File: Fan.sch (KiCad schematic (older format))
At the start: 11 parts, among them Q2 DMN65D8L-7, Q3 AOD476, Q4 AOD476, U4 OPA4170, U5 MCP4801

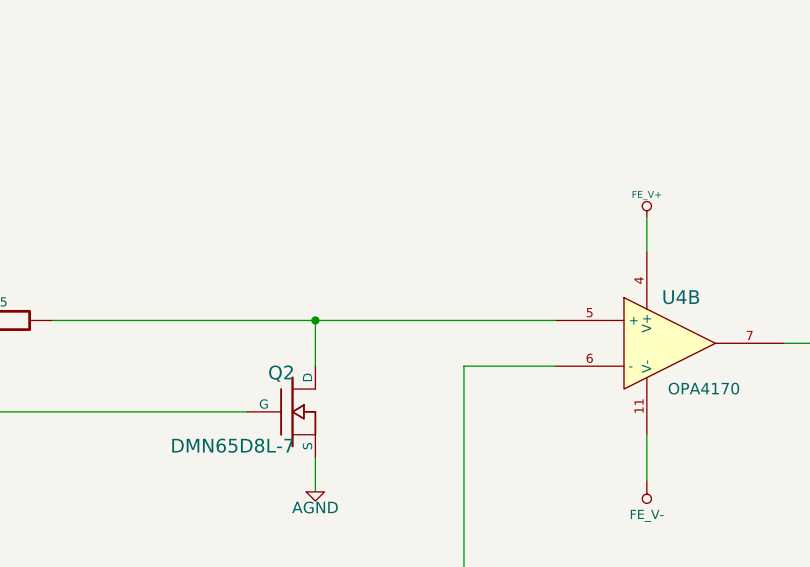
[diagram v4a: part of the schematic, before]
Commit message: Layout Work Session 18 Output
Added test points, changed a bunch of silk screen, added another
mounting hole and added a placeholder for the final commit number of the
board being sent to fab.
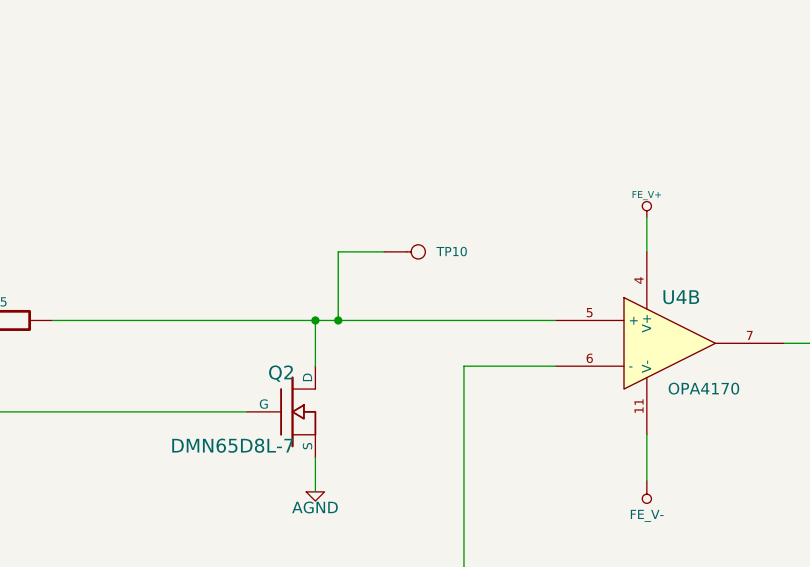
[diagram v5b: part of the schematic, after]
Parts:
- added TP10: DAC_OUT, symbol CONN_1
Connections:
- net at Q2.2 (D), R15.2, U4.5 (+): now also TP10.1
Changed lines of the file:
@@
-EESchema Schematic File Version 2  date 12/3/2013 1:00:45 AM
+EESchema Schematic File Version 2  date 12/18/2013 11:27:15 PM
 LIBS:power
 LIBS:device
@@
 Sheet 6 9
 Title ""
-Date "3 dec 2013"
+Date "19 dec 2013"
 Rev ""
 Comp ""
@@
 	1    0    0    -1
 $EndComp
+$Comp
+L CONN_1 TP10
+U 1 1 52B283CC
+P 5150 2700
+F 0 "TP10" H 5230 2700 40  0000 L CNN
+F 1 "DAC_OUT" H 5150 2755 30  0001 C CNN
+F 2 "" H 5150 2700 60  0000 C CNN
+F 3 "" H 5150 2700 60  0000 C CNN
+	1    5150 2700
+	1    0    0    -1
+$EndComp
+Wire Wire Line
+	5000 2700 4800 2700
+Wire Wire Line
+	4800 2700 4800 3000
+Connection ~ 4800 3000
 $EndSCHEMATC

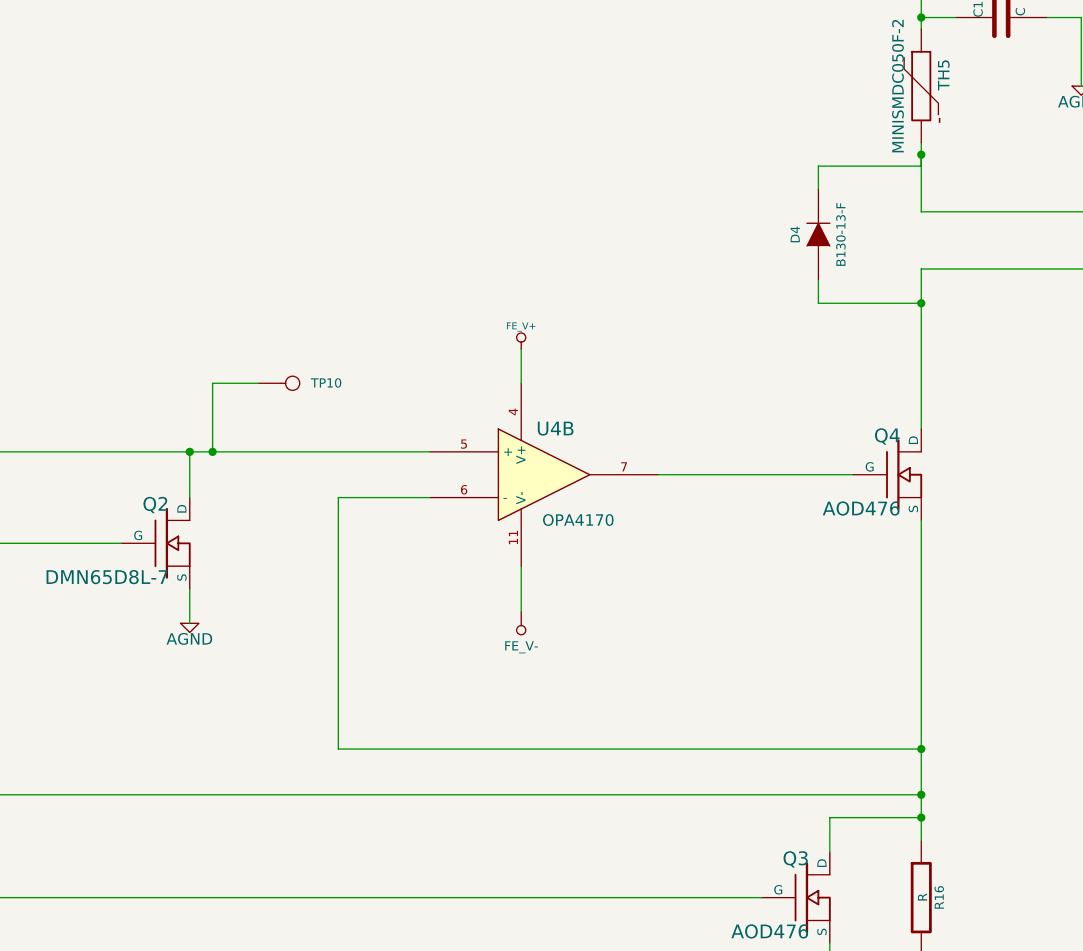
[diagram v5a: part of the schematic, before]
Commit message: Analog IO Cleanup/Additions
Added some placed holder caps and resistors
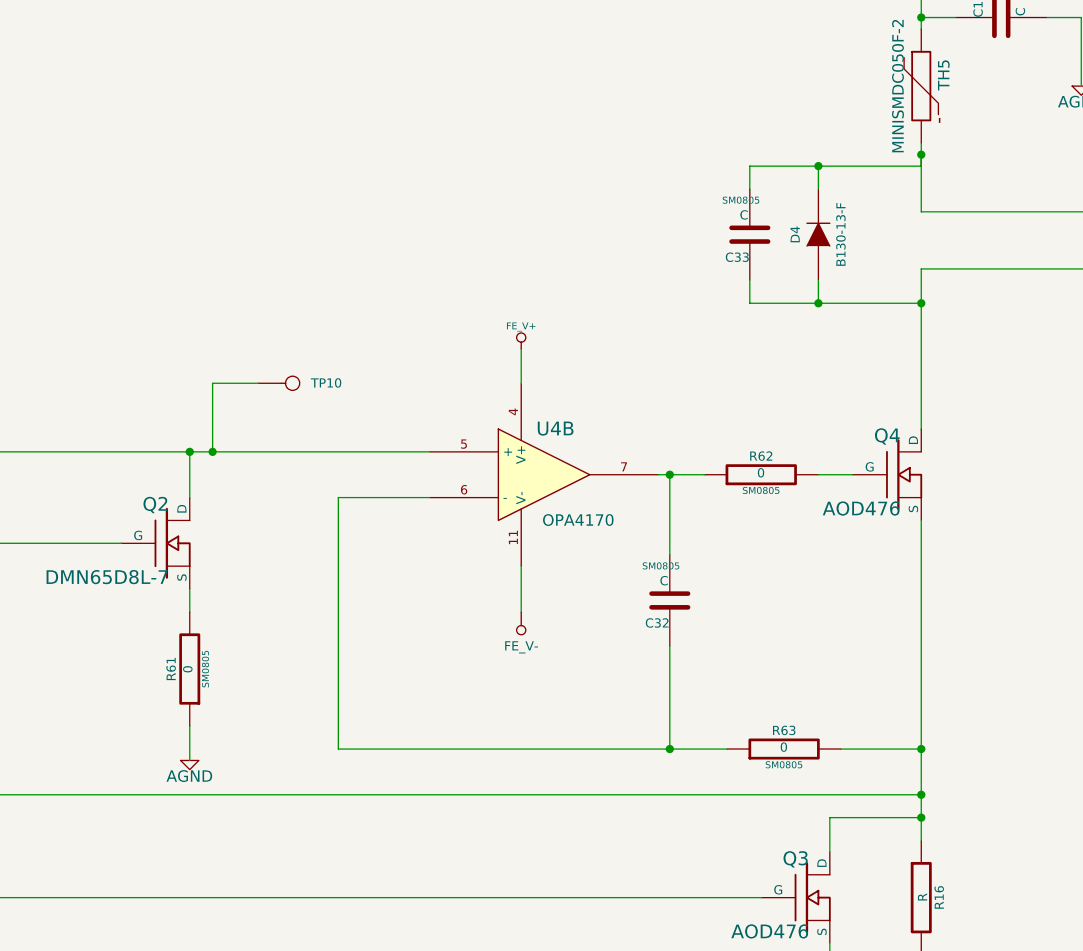
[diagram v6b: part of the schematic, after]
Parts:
- added C32, C33: C, SM0805, symbol C
- added R61, R62, R63: 0, SM0805, symbol R
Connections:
- net AGND: now also R61.1; no longer Q2.3 (S)
- net CURR_MEAS: now also R63.2; no longer U4.6 (-)
- net FAN_OUT+: now also C33.2
- net FAN_OUT-: now also C33.1
- net at U4.7: now also C32.2, R62.1; no longer Q4.1 (G)
- new net: C32.1, R63.1, U4.6 (-)
- new net: Q2.3 (S), R61.2
- new net: Q4.1 (G), R62.2
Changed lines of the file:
@@
-EESchema Schematic File Version 2  date 12/18/2013 11:27:15 PM
+EESchema Schematic File Version 2  date 2/16/2014 3:41:32 PM
 LIBS:power
 LIBS:device
@@
 Sheet 6 9
 Title ""
-Date "19 dec 2013"
+Date "16 feb 2014"
 Rev ""
 Comp ""
@@
 $EndComp
 Wire Wire Line
-	7600 3100 6750 3100
-Wire Wire Line
 	7900 3300 7900 4700
 Wire Wire Line
@@
 	3550 3000 5750 3000
 Wire Wire Line
-	4700 3600 4700 3750
-Wire Wire Line
 	1450 4500 7900 4500
 Connection ~ 7900 4500
@@
 	7900 2200 7900 2900
 Wire Wire Line
-	7900 2350 7450 2350
+	7150 2350 7900 2350
 Wire Wire Line
 	7450 2350 7450 2250
@@
 	7450 1850 7450 1750
 Wire Wire Line
-	7450 1750 7900 1750
+	7150 1750 7900 1750
 Wire Wire Line
 	7900 1750 7900 1700
 Connection ~ 7900 1700
-Wire Wire Line
-	5350 4300 7900 4300
 Wire Wire Line
 	7500 4750 7500 4600
@@
 FAN_MODE
 $Comp
-L +12C #PWR43
+L +12C #PWR032
 U 1 1 5243907A
 P 7900 1000
-F 0 "#PWR43" H 7900 970 30  0001 C CNN
+F 0 "#PWR032" H 7900 970 30  0001 C CNN
 F 1 "+12C" H 7900 1110 40  0000 C CNN
 F 2 "~" H 7900 1000 60  0000 C CNN
@@
 	1350 1950 1500 1950
 $Comp
-L +5V #PWR38
+L +5V #PWR033
 U 1 1 525C1500
 P 2000 1700
-F 0 "#PWR38" H 2000 1790 20  0001 C CNN
+F 0 "#PWR033" H 2000 1790 20  0001 C CNN
 F 1 "+5V" H 2000 1790 30  0000 C CNN
 F 2 "~" H 2000 1700 60  0000 C CNN
@@
 $EndComp
 $Comp
-L FE_V+ #PWR41
+L FE_V+ #PWR034
 U 1 1 526E03BB
 P 6150 2550
-F 0 "#PWR41" H 6150 2650 30  0001 C CNN
+F 0 "#PWR034" H 6150 2650 30  0001 C CNN
 F 1 "FE_V+" H 6150 2650 30  0000 C CNN
 F 2 "~" H 6150 2550 60  0000 C CNN
@@
 	6150 2700 6150 2550
 $Comp
-L AGND #PWR40
+L AGND #PWR035
 U 1 1 527EEACF
-P 4700 3750
-F 0 "#PWR40" H 4700 3750 40  0001 C CNN
-F 1 "AGND" H 4700 3680 50  0000 C CNN
-F 2 "~" H 4700 3750 60  0000 C CNN
-F 3 "~" H 4700 3750 60  0000 C CNN
-	1    4700 3750
-	1    0    0    -1
-$EndComp
-$Comp
-L AGND #PWR44
+P 4700 4350
+F 0 "#PWR035" H 4700 4350 40  0001 C CNN
+F 1 "AGND" H 4700 4280 50  0000 C CNN
+F 2 "~" H 4700 4350 60  0000 C CNN
+F 3 "~" H 4700 4350 60  0000 C CNN
+	1    4700 4350
+	1    0    0    -1
+$EndComp
+$Comp
+L AGND #PWR036
 U 1 1 527EEAEB
 P 7900 5550
-F 0 "#PWR44" H 7900 5550 40  0001 C CNN
+F 0 "#PWR036" H 7900 5550 40  0001 C CNN
 F 1 "AGND" H 7900 5480 50  0000 C CNN
 F 2 "~" H 7900 5550 60  0000 C CNN
@@
 $EndComp
 $Comp
-L AGND #PWR39
+L AGND #PWR037
 U 1 1 527EEAF1
 P 2000 3950
-F 0 "#PWR39" H 2000 3950 40  0001 C CNN
+F 0 "#PWR037" H 2000 3950 40  0001 C CNN
 F 1 "AGND" H 2000 3880 50  0000 C CNN
 F 2 "~" H 2000 3950 60  0000 C CNN
@@
 $EndComp
 $Comp
-L AGND #PWR37
+L AGND #PWR038
 U 1 1 527EEAF7
 P 1350 2050
-F 0 "#PWR37" H 1350 2050 40  0001 C CNN
+F 0 "#PWR038" H 1350 2050 40  0001 C CNN
 F 1 "AGND" H 1350 1980 50  0000 C CNN
 F 2 "~" H 1350 2050 60  0000 C CNN
@@
 $EndComp
 $Comp
-L AGND #PWR45
+L AGND #PWR039
 U 1 1 527EEAFD
 P 8600 1400
-F 0 "#PWR45" H 8600 1400 40  0001 C CNN
+F 0 "#PWR039" H 8600 1400 40  0001 C CNN
 F 1 "AGND" H 8600 1330 50  0000 C CNN
 F 2 "~" H 8600 1400 60  0000 C CNN
@@
 	4800 2700 4800 3000
 Connection ~ 4800 3000
+$Comp
+L R R62
+U 1 1 5301A403
+P 7200 3100
+F 0 "R62" V 7280 3100 40  0000 C CNN
+F 1 "0" V 7207 3101 40  0000 C CNN
+F 2 "SM0805" V 7130 3100 30  0000 C CNN
+F 3 "~" H 7200 3100 30  0000 C CNN
+	1    7200 3100
+	0    -1   -1   0
+$EndComp
+Wire Wire Line
+	6950 3100 6750 3100
+Wire Wire Line
+	7450 3100 7600 3100
+$Comp
+L C C32
+U 1 1 5301A4CA
+P 6800 3650
+F 0 "C32" H 6800 3750 40  0000 L CNN
+F 1 "C" H 6806 3565 40  0000 L CNN
+F 2 "SM0805" H 6838 3500 30  0000 C CNN
+F 3 "~" H 6800 3650 60  0000 C CNN
+	1    6800 3650
+	-1   0    0    1
+$EndComp
+Wire Wire Line
+	6800 3100 6800 3450
+Connection ~ 6800 3100
+Wire Wire Line
+	6800 3850 6800 4300
+Connection ~ 6800 4300
+$Comp
+L R R63
+U 1 1 5301A5DD
+P 7300 4300
+F 0 "R63" V 7380 4300 40  0000 C CNN
+F 1 "0" V 7307 4301 40  0000 C CNN
+F 2 "SM0805" V 7230 4300 30  0000 C CNN
+F 3 "~" H 7300 4300 30  0000 C CNN
+	1    7300 4300
+	0    -1   -1   0
+$EndComp
+Wire Wire Line
+	7900 4300 7550 4300
+Wire Wire Line
+	5350 4300 7050 4300
+$Comp
+L C C33
+U 1 1 5301A6BE
+P 7150 2050
+F 0 "C33" H 7150 2150 40  0000 L CNN
+F 1 "C" H 7156 1965 40  0000 L CNN
+F 2 "SM0805" H 7188 1900 30  0000 C CNN
+F 3 "~" H 7150 2050 60  0000 C CNN
+	1    7150 2050
+	-1   0    0    1
+$EndComp
+Wire Wire Line
+	7150 1750 7150 1850
+Connection ~ 7450 1750
+Wire Wire Line
+	7150 2250 7150 2350
+Connection ~ 7450 2350
+$Comp
+L R R61
+U 1 1 5301A7E0
+P 4700 3950
+F 0 "R61" V 4780 3950 40  0000 C CNN
+F 1 "0" V 4707 3951 40  0000 C CNN
+F 2 "SM0805" V 4630 3950 30  0000 C CNN
+F 3 "~" H 4700 3950 30  0000 C CNN
+	1    4700 3950
+	-1   0    0    1
+$EndComp
+Wire Wire Line
+	4700 3600 4700 3700
+Wire Wire Line
+	4700 4200 4700 4350
 $EndSCHEMATC

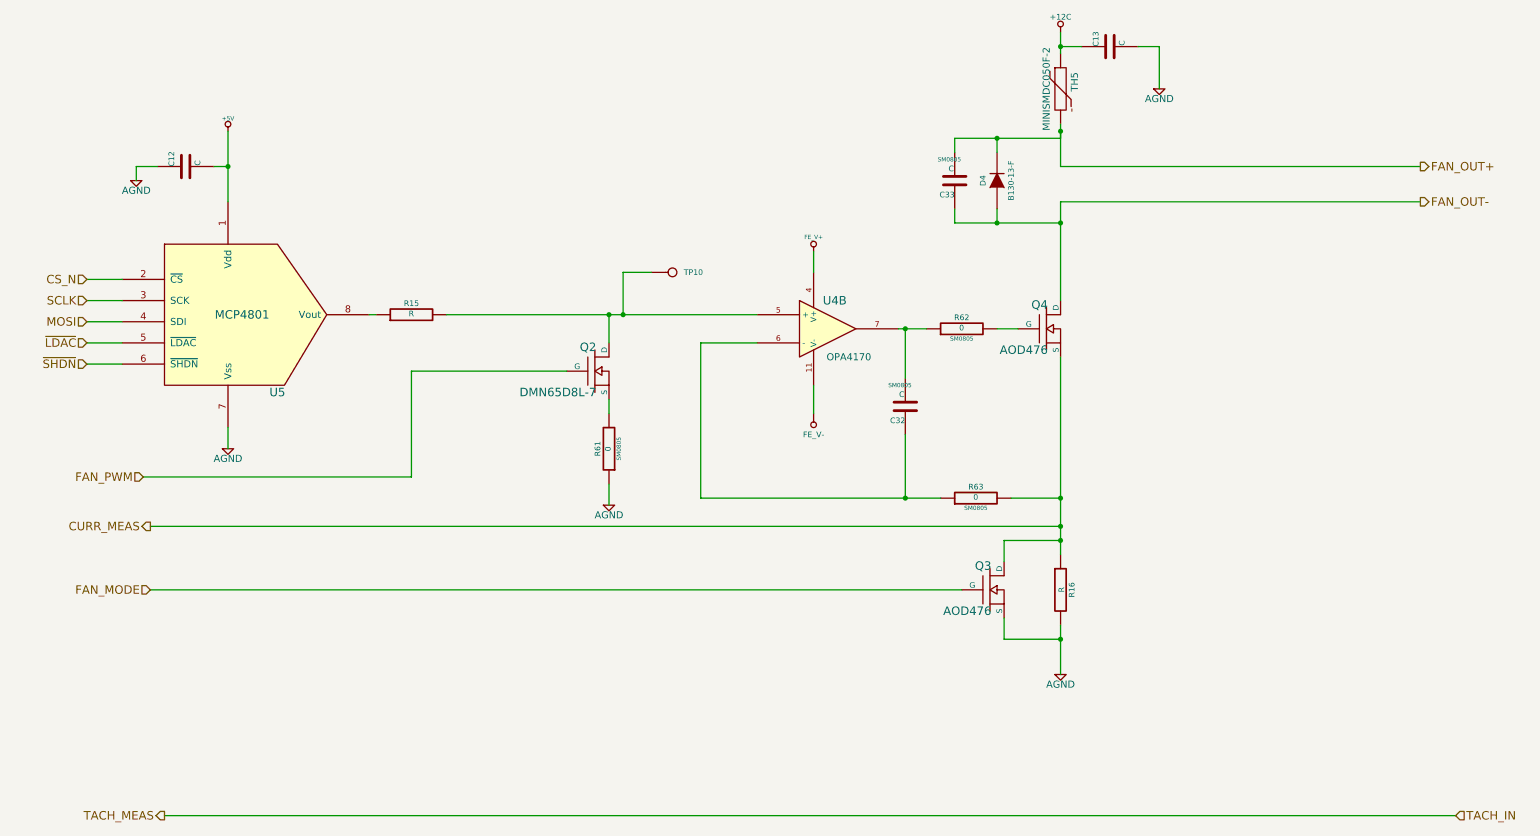
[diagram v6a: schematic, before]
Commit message: Added Passive Values and SPICE models
As part of week 1 of Session 1B, we added a SPICE model of the In amp
and went through and assigned values to all of the passive components.
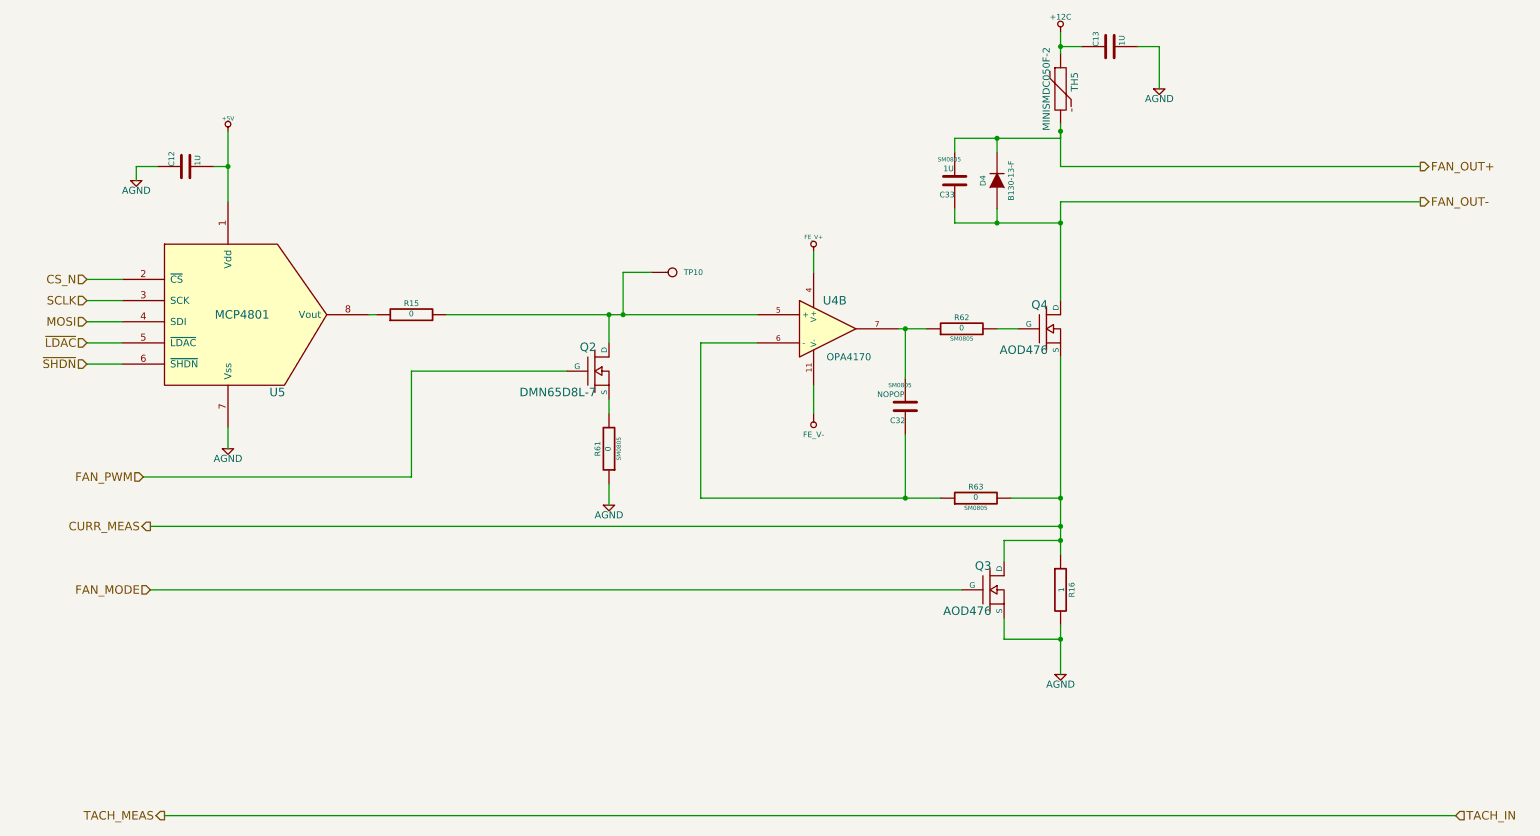
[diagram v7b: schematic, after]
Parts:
- C12, C13, C33: value C -> 1U
- C32: value C -> NOPOP
- R15: value R -> 0
- R16: value R -> 1
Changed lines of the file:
@@
-EESchema Schematic File Version 2  date 2/16/2014 3:41:32 PM
+EESchema Schematic File Version 2  date 4/16/2014 11:04:06 PM
 LIBS:power
 LIBS:device
@@
 Sheet 6 9
 Title ""
-Date "16 feb 2014"
+Date "17 apr 2014"
 Rev ""
 Comp ""
@@
 P 7900 4950
 F 0 "R16" V 7980 4950 40  0000 C CNN
-F 1 "R" V 7907 4951 40  0000 C CNN
+F 1 "1" V 7907 4951 40  0000 C CNN
 F 2 "~" V 7830 4950 30  0000 C CNN
 F 3 "~" H 7900 4950 30  0000 C CNN
@@
 P 3300 3000
 F 0 "R15" V 3380 3000 40  0000 C CNN
-F 1 "R" V 3307 3001 40  0000 C CNN
+F 1 "0" V 3307 3001 40  0000 C CNN
 F 2 "~" V 3230 3000 30  0000 C CNN
 F 3 "~" H 3300 3000 30  0000 C CNN
@@
 P 1700 1950
 F 0 "C12" H 1700 2050 40  0000 L CNN
-F 1 "C" H 1706 1865 40  0000 L CNN
+F 1 "1U" H 1706 1865 40  0000 L CNN
 F 2 "~" H 1738 1800 30  0000 C CNN
 F 3 "~" H 1700 1950 60  0000 C CNN
@@
 P 8250 1100
 F 0 "C13" H 8250 1200 40  0000 L CNN
-F 1 "C" H 8256 1015 40  0000 L CNN
+F 1 "1U" H 8256 1015 40  0000 L CNN
 F 2 "~" H 8288 950 30  0000 C CNN
 F 3 "~" H 8250 1100 60  0000 C CNN
@@
 P 6800 3650
 F 0 "C32" H 6800 3750 40  0000 L CNN
-F 1 "C" H 6806 3565 40  0000 L CNN
+F 1 "NOPOP" H 6806 3565 40  0000 L CNN
 F 2 "SM0805" H 6838 3500 30  0000 C CNN
 F 3 "~" H 6800 3650 60  0000 C CNN
@@
 P 7150 2050
 F 0 "C33" H 7150 2150 40  0000 L CNN
-F 1 "C" H 7156 1965 40  0000 L CNN
+F 1 "1U" H 7156 1965 40  0000 L CNN
 F 2 "SM0805" H 7188 1900 30  0000 C CNN
 F 3 "~" H 7150 2050 60  0000 C CNN
